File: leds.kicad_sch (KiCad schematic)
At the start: 9 parts, among them U15 XL-1010RGBC-WS2812B, U16 XL-1010RGBC-WS2812B, U17 XL-1010RGBC-WS2812B, U18 XL-1010RGBC-WS2812B, U3 XL-1010RGBC-WS2812B, U4 XL-1010RGBC-WS2812B, U5 XL-1010RGBC-WS2812B, U8 XL-1010RGBC-WS2812B

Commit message: Final routing
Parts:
- added U22, U23, U24, U25, U26, U27, U28, U29: XL-1010RGBC-WS2812B, lib:LED-SMD_4P-L1.0-W1.0-TL_XL-1010RGBC-WS2812B, symbol lib:XL-1010RGBC-WS2812B
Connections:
- net +4.5V: now also U22.2 (VDD), U23.2 (VDD), U24.2 (VDD), U25.2 (VDD), U26.2 (VDD), U27.2 (VDD), U28.2 (VDD), U29.2 (VDD)
- net GND: now also U22.3 (GND), U23.3 (GND), U24.3 (GND), U25.3 (GND), U26.3 (GND), U27.3 (GND), U28.3 (GND), U29.3 (GND)
- net at U5.1 (DOUT), U8.4 (DIN): now also U24.4 (DIN)
- net at U4.1 (DOUT), U5.4 (DIN): now also U23.4 (DIN)
- net at U15.1 (DOUT), U16.4 (DIN): now also U26.4 (DIN)
- net at U15.4 (DIN), U8.1 (DOUT): now also U25.4 (DIN)
- net at U18.1 (DOUT): now also U29.4 (DIN)
- net at U17.1 (DOUT), U18.4 (DIN): now also U28.4 (DIN)
- net at U16.1 (DOUT), U17.4 (DIN): now also U27.4 (DIN)
- net at U3.1 (DOUT), U4.4 (DIN): now also U22.4 (DIN)
- no-connect marks 1 -> 8
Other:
- note added: "4 LED's on each corner"
- note removed: "2 LED's on each corner"

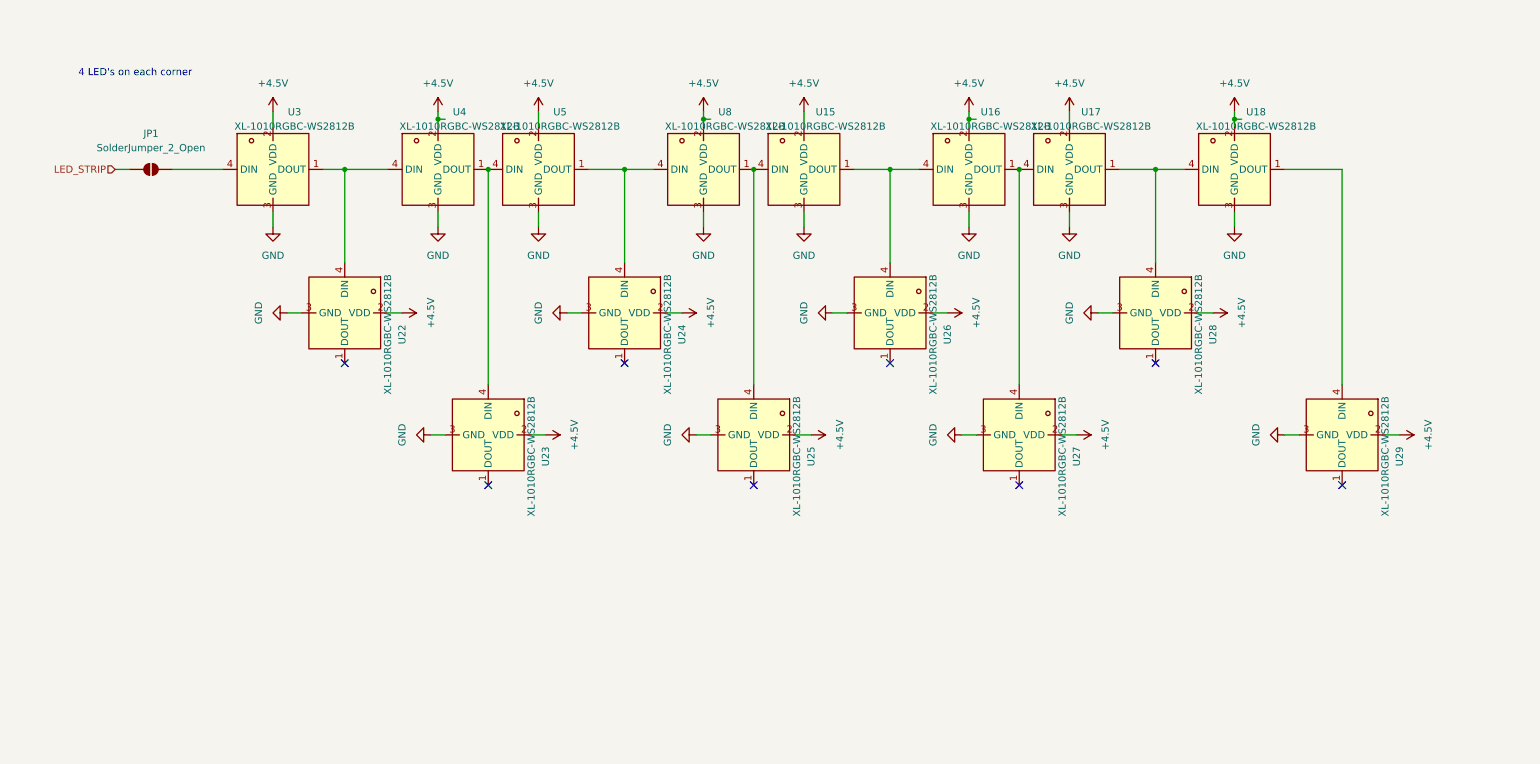
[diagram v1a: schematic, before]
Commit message: Added Open-OSD-X and new layout
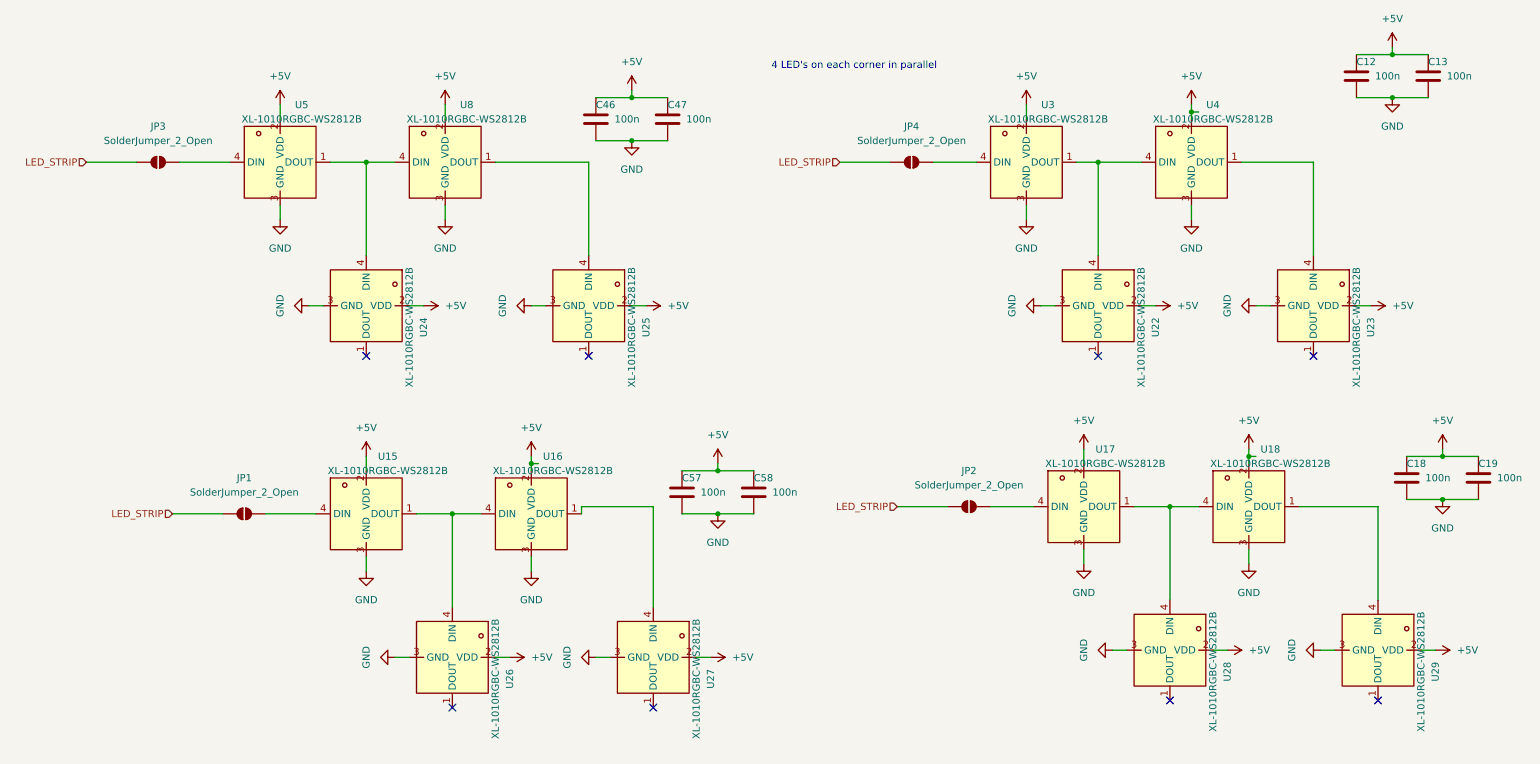
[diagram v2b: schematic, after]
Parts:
- added C12, C13, C18, C19, C46, C47, C57, C58: 100n, Capacitor_SMD:C_0402_1005Metric, symbol Device:C
- added JP2, JP3, JP4: SolderJumper_2_Open, Panelization:MouseBite-Slot-Jumper_0201, symbol Jumper:SolderJumper_2_Open
- JP1: footprint Jumper:SolderJumper-2_P1.3mm_Open_TrianglePad1.0x1.5mm -> Panelization:MouseBite-Slot-Jumper_0201
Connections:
- net GND: now also C12.2, C13.2, C18.2, C19.2, C46.2, C47.2, C57.2, C58.2
- net LED_STRIP: now also JP2.1 (A), JP3.1 (A), JP4.1 (A)
- net at U25.4 (DIN), U8.1 (DOUT): no longer U15.4 (DIN)
- net at U23.4 (DIN), U4.1 (DOUT): no longer U5.4 (DIN)
- net at U16.1 (DOUT), U27.4 (DIN): no longer U17.4 (DIN)
- net at JP1.2 (B): now also U15.4 (DIN); no longer U3.4 (DIN)
- net +4.5V renamed +5V
- net +5V: now also C12.1, C13.1, C18.1, C19.1, C46.1, C47.1, C57.1, C58.1
- new net: JP3.2 (B), U5.4 (DIN)
- new net: JP2.2 (B), U17.4 (DIN)
- new net: JP4.2 (B), U3.4 (DIN)
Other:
- note added: "4 LED's on each corner in parallel"
- note removed: "4 LED's on each corner"
- moved on the sheet: U15, U16, U17, U18, U22, U23, U24, U25, U26, U27, U28, U29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
